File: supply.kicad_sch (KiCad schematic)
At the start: 78 parts, among them U1 AP7330-W5-7, U2 AP7330-W5-7, U3 AP7330-W5-7, U4 AP62301WU-7, U5 AP62301WU-7, U6 AP62301WU-7, U8 NCV51200MNTXG

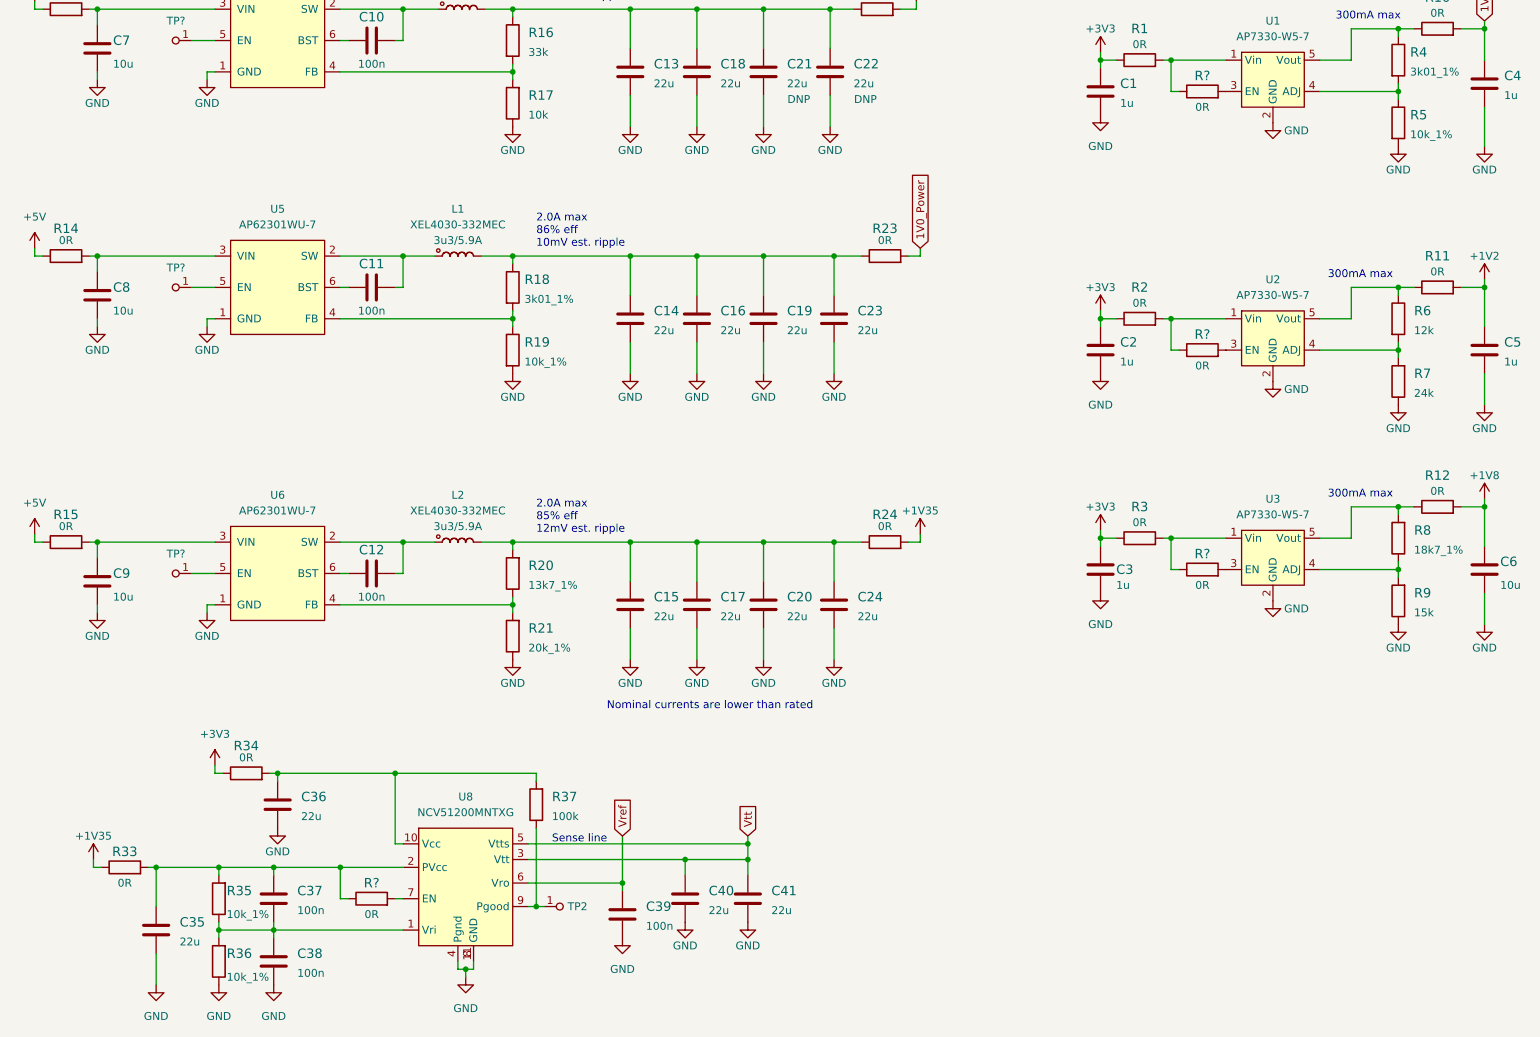
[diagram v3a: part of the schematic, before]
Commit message: Added power testpoints
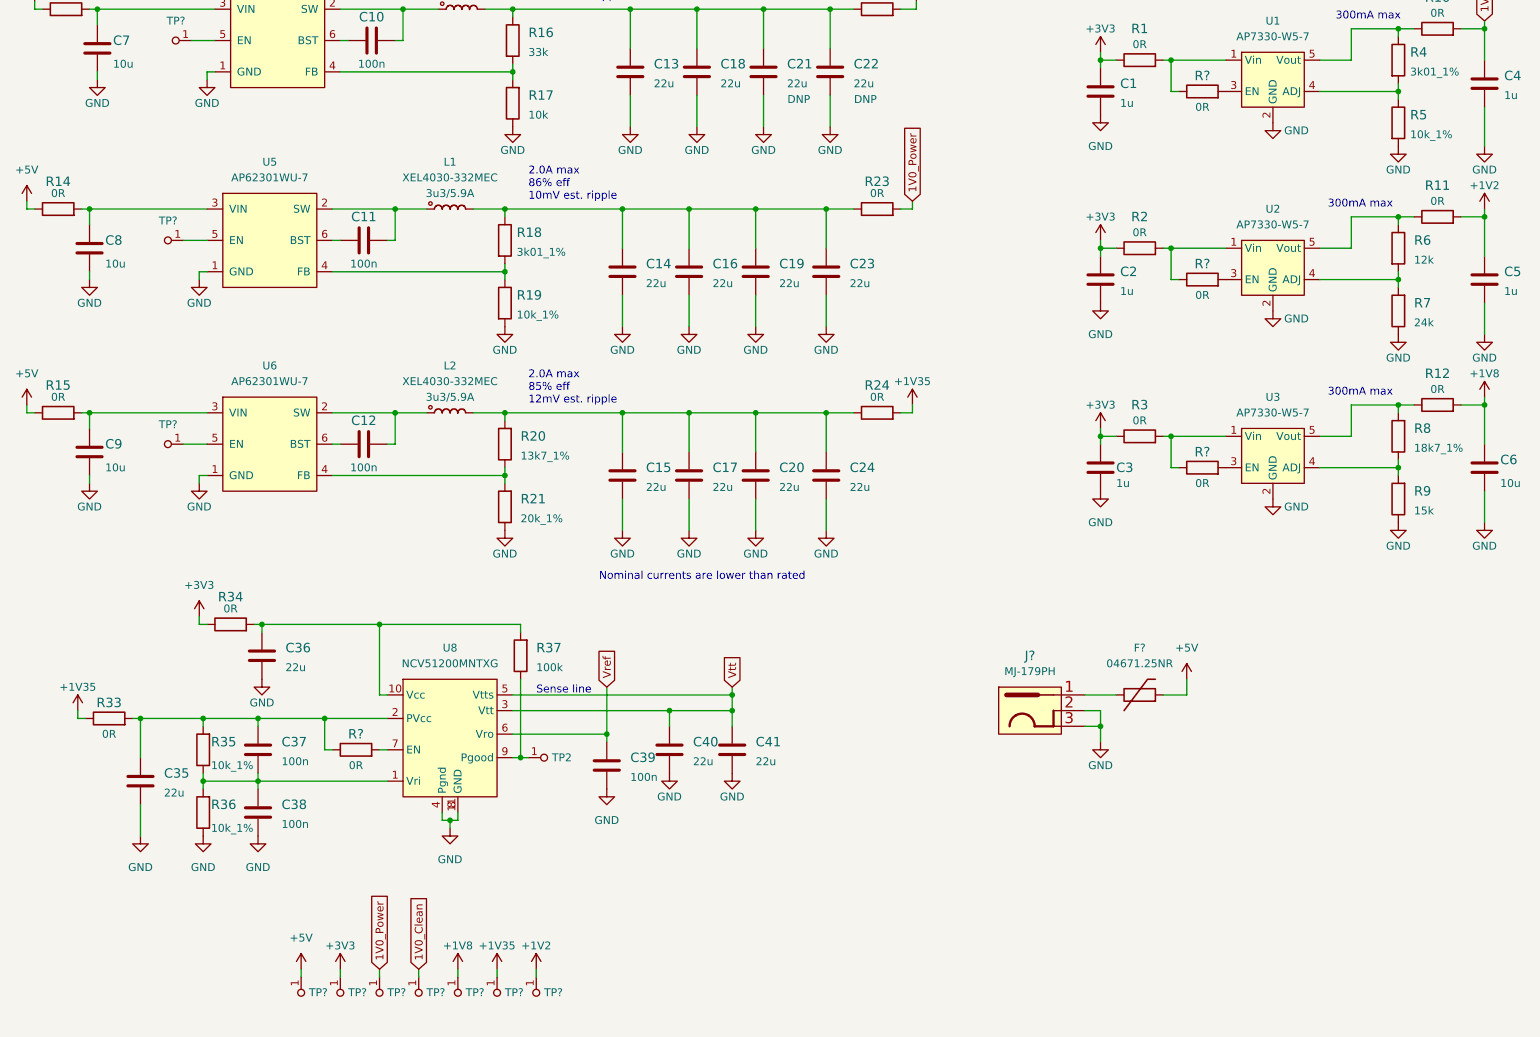
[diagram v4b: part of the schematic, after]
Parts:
- added F?: 04671.25NR, antmicro-footprints:0603-Fuse-Littelfuse-0467, symbol antmicroFuses:04671.25NR
- added J?: DC_SOCKET, antmicro-footprints:DC_SOCKET, symbol antmicroBarrelAudioConnectors:DC_SOCKET
- added TP? (x7): TP, antmicro-footprints:TP-R-1.5, symbol antmicroTestPoints:TP
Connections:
- net +1V2: now also TP?.1
- net +1V35: now also TP?.1
- net +1V8: now also TP?.1
- net +3V3: now also TP?.1
- net +5V: now also F?.2, TP?.1
- net 1V0_Clean: now also TP?.1
- net 1V0_Power: now also TP?.1
- net GND: now also J?.2, J?.3
- new net: F?.1, J?.1
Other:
- moved on the sheet: C11, C12, C14, C15, C16, C17, C19, C2, C20, C23, C24, C3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
